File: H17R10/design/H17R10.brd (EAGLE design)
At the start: 60.6 x 60 mm, 94 parts, among them P1 HEXABIT__X3_NO_P1_P2_P3_P4_P5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, P4 PAD4, P5 PAD4, P6 PAD4, U1 STM32F091RBT6STMICROELECTRONI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, U3 TEXAS_INSTRUMENTS_ISO7741DBQR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, U4 TEXAS_INSTRUMENTS_ISO7742DBQR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, X1 XTALL_CSTCE8M00G52

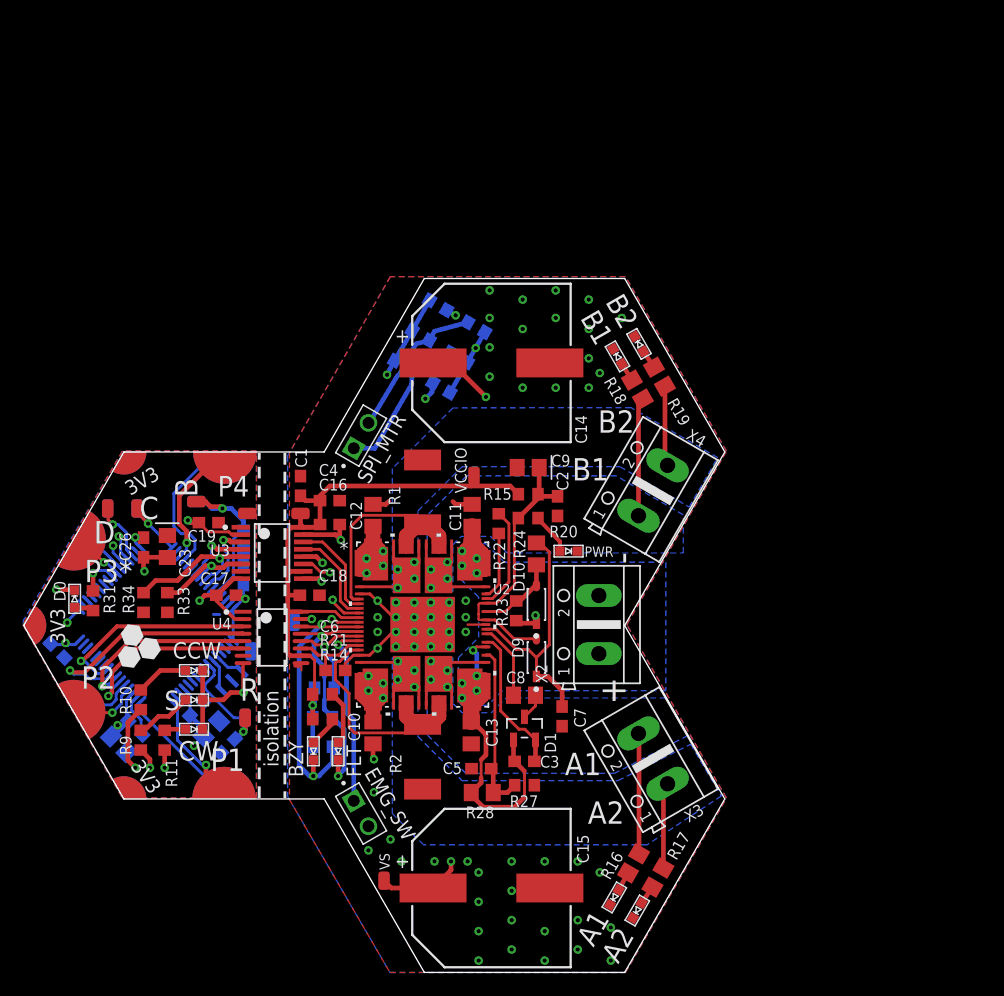
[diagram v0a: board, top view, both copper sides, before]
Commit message: -Changing the MCU to STM32G0B1CEU6N -Editing the electronic design -Editing the layout design to improve the performance
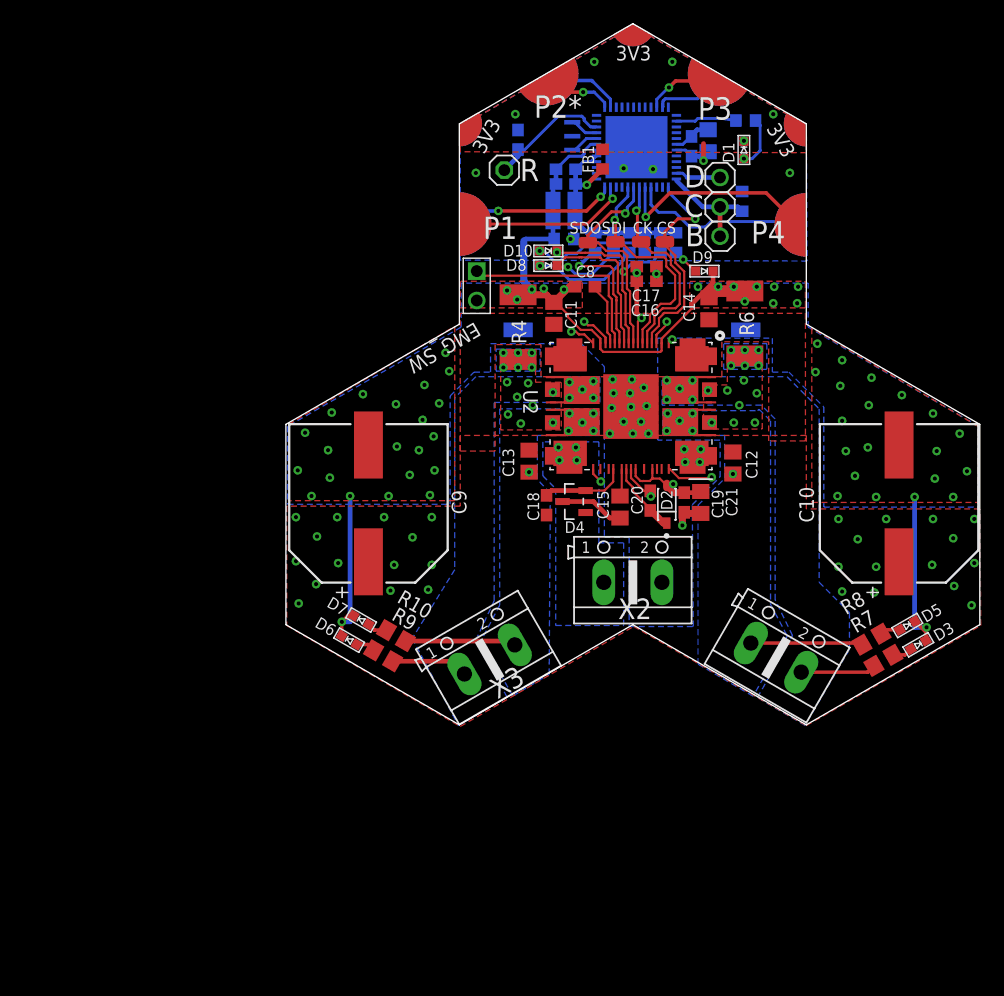
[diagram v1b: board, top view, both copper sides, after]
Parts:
- removed A1, A2, B1, B2, BZY: YELLOW, HEXABITZ_USER_INTERFACE_PARTS:VLMY1300-GS08
- removed B, C, D, R: PAD1, Hexabitz:PAD1
- removed C22: 1.00uF, Hexabitz:C-0805-POL
- removed C23, C24: 4.7uF, Hexabitz:C-0805-POL
- removed C25: 10nF, Hexabitz:C-0603
- removed C26, C27, C28, C29: 100nF, Hexabitz:C-0603
- removed CCW, CW, PWR: Green, HEXABITZ_USER_INTERFACE_PARTS:VLMTG1300-GS08
- removed D0, FLT, S: RED, HEXABITZ_USER_INTERFACE_PARTS:VLMS1300-GS08
- removed EMG_SW, SPI_MTR: 3-644456-2, HEXABITZ_USER_INTERFACE_PARTS:TE_3-644456-2
- removed P1: HEXABIT__X3_NO_P1_P2_P3_P4_P5_P6_P11_P12, hexabitz_connectors:HEXABIT_17.32_X3_NO_P1_P2_P3_P4_P5_P6_P11_P12
- removed P4, P5, P6, VCCIO, VCCIO1, VS: PAD4, HEXABITZ_CONNECTION_PARTS:PAD4
- removed R16, R17, R18, R19: 10k, HEXABITZ_RCLS:R-0805
- removed R20, R21: 330, HEXABITZ_RCLS:R-0603
- removed R22, R27, R33, R34: DNP, HEXABITZ_RCLS:R-0603
- removed R23: 0R, HEXABITZ_RCLS:R-0603
- removed R24, R28: DNP, HEXABITZ_RCLS:R-0805
- removed R25, R26: 39K, HEXABITZ_RCLS:R-0603
- removed R31: 270.0R, HEXABITZ_RCLS:R-0603
- removed R32: 10.0K, Hexabitz:R-0603
- removed U3: TEXAS_INSTRUMENTS_ISO7741DBQRTEXAS_INSTRUMENTS_ISO7741DBQR_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, HEXABITZ_ICs:TEXAS_INSTRUMENTS_ISO7741DBQR_0
- removed U4: TEXAS_INSTRUMENTS_ISO7742DBQRTEXAS_INSTRUMENTS_ISO7742DBQR_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, Texas Instruments - ISO7742DBQR:TEXAS_INSTRUMENTS_ISO7742DBQR_3
- added C20: 470nF, HEXABITZ_RCLS:C-0603
- added CK, CS, SDI, SDO: PAD4, HEXABITZ_CONNECTION_PARTS:PAD4
- added D2: STMICROELECTRONICS_BAT46ZFILMSTMICROELECTRONICS_BAT46ZFILM_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, HEXABITZ_RCLS:STMICROELECTRONICS_BAT46ZFILM_3
- added D3, D5, D6, D7: YELLOW, HEXABITZ_USER_INTERFACE_PARTS:VLMY1300-GS08
- added D4: STMICROELECTRONICS_BAR43SFILMSTMICROELECTRONICS_BAR43SFILM_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, HEXABITZ_RCLS:STMICROELECTRONICS_BAR43SFILM_0
- added D8: RED, HEXABITZ_USER_INTERFACE_PARTS:VLMS1300-GS08
- added FB1: (no value), HEXABITZ_RCLS:FB-TDK_MMZ1608Y300B
- added J1: 3-644456-2, HEXABITZ_USER_INTERFACE_PARTS:TE_3-644456-2
- added JP1: (no value), HEXABITZ_USER_INTERFACE_PARTS:1X01
- added JP2: (no value), pinhead:1X03
- added R12: 330, HEXABITZ_RCLS:R-0603
- added SJ1, SJ2: (no value), jumper:SJW
- added U$1: HEXABIT_17.32_X3_NO_P1_P2_P3_P4_P5_P6_P11_P12, hexabitz_connectors:HEXABIT_17.32_X3_NO_P1_P2_P3_P4_P5_P6_P11_P12
- C10: value 220nF -> 68uF; device HEXABITZ_RCLS:C-0805 -> HEXABITZ_RCLS:WCAP-ASLI_12.5X14(DXL)
- C14: value 68uF -> 220nF; device HEXABITZ_RCLS:WCAP-ASLI_12.5X14(DXL) -> HEXABITZ_RCLS:C-0805
- C15: value 68uF -> 47nF; device HEXABITZ_RCLS:WCAP-ASLI_12.5X14(DXL) -> HEXABITZ_RCLS:C-0805
- C18: value 100nF -> 470nF
- C19: value 100nF -> 220nF
- C2: value 220nF -> 100nF
- C21: value 100nF -> 22uF; device HEXABITZ_RCLS:C-0603 -> HEXABITZ_RCLS:C-0805-POL
- C3, C7: value 470nF -> 4.7uF; device HEXABITZ_RCLS:C-0603 -> HEXABITZ_RCLS:C-0805-POL
- C4: value 3.3nF -> 100nF
- C5: value DNP -> 1uF; device HEXABITZ_RCLS:C-0603 -> HEXABITZ_RCLS:C-0805-POL
- C8: value 47nF -> 100nF; device HEXABITZ_RCLS:C-0805 -> HEXABITZ_RCLS:C-0603
- C9: value 22uF -> 68uF; device HEXABITZ_RCLS:C-0805-POL -> HEXABITZ_RCLS:WCAP-ASLI_12.5X14(DXL)
- D1: value STMICROELECTRONICS_BAR43SFILMSTMICROELECTRONICS_BAR43SFILM_0_0 -> RED; device HEXABITZ_RCLS:STMICROELECTRONICS_BAR43SFILM_0 -> HEXABITZ_USER_INTERFACE_PARTS:VLMS1300-GS08
- D10: value STMICROELECTRONICS_BAT46ZFILMSTMICROELECTRONICS_BAT46ZFILM_0_3 -> YELLOW; device HEXABITZ_RCLS:STMICROELECTRONICS_BAT46ZFILM_3 -> HEXABITZ_USER_INTERFACE_PARTS:VLMY1300-GS08
- D9: value STMICROELECTRONICS_BAT46ZFILMSTMICROELECTRONICS_BAT46ZFILM_0_3 -> Green; device HEXABITZ_RCLS:STMICROELECTRONICS_BAT46ZFILM_3 -> HEXABITZ_USER_INTERFACE_PARTS:VLMTG1300-GS08
- R1: value 0R1 -> 0.0R; device HEXABITZ_RCLS:R2512 -> HEXABITZ_RCLS:R-0603
- R10, R9: value 270.0R -> 10k; device HEXABITZ_RCLS:R-0603 -> HEXABITZ_RCLS:R-0805
- R11: value 270.0R -> 330
- R14: value 330 -> 39K
- R15: value 0R -> 330
- R2: value 0R1 -> 270R; device HEXABITZ_RCLS:R2512 -> HEXABITZ_RCLS:R-0603
- R3: value 0R -> 10K
- R4, R6: value DNP -> 0R1; device HEXABITZ_RCLS:R-0603 -> HEXABITZ_RCLS:R2512
- R5: value DNP -> 39K
- R7: value DNP -> 10k; device HEXABITZ_RCLS:R-0603 -> HEXABITZ_RCLS:R-0805
- R8: value 0R -> 10k; device HEXABITZ_RCLS:R-0603 -> HEXABITZ_RCLS:R-0805
- U1: value STM32F091RBT6STMICROELECTRONICS_STM32F091RBT6_0_1 -> STM32G0B1CEU6NUFQFPN48_STM32_STM; device Hexabitz:STMICROELECTRONICS_STM32F091RBT6_1 -> HEXABITZ_ICs:UFQFPN48_STM32_STM
- U2: value (none) -> POWERSTEP01; device HEXABITZ_ICs:VFQFPN89_11X14X1_STM -> POWERSTEP01:IC_POWERSTEP01
- X1: value XTALL_CSTCE8M00G52 -> 8MHZ; device Hexabitz:XTALL_CSTCE8M00G52 -> HEXABITZ_OTHER_PARTS:XTALL_CSTCE8M00G52
- moved R2 61.7 mm to (9.76, 43.6), flipped to the bottom, turned to 0 degrees
- moved R11 58.9 mm to (-0.32, 33.0), flipped to the bottom, turned to 90 degrees
- moved U1 58.5 mm to (0.32, 41.3), turned to 180 degrees
- moved X1 55.5 mm to (-5.24, 42.2), turned to 180 degrees
- moved C6 54.8 mm to (5.08, 41.4), flipped to the bottom, turned to 270 degrees
- moved D1 53.5 mm to (9.60, 41.0), turned to 180 degrees
- moved C7 51.3 mm to (6.51, 41.8), flipped to the bottom, turned to 90 degrees
- moved R14 50.5 mm to (2.38, 33.0), flipped to the bottom, turned to 90 degrees
- moved C10 49.6 mm to (23.0, 10.5)
- moved C3 48.6 mm to (-5.95, 36.7), flipped to the bottom, turned to 0 degrees
- moved R13 48.1 mm to (-1.67, 33.0), turned to 90 degrees
- moved C5 47.9 mm to (-5.95, 34.9), flipped to the bottom, turned to 0 degrees
- moved C17 46.1 mm to (1.19, 31.0)
- moved C21 46.0 mm to (5.87, 10.6), flipped to the top, turned to 270 degrees
- moved R7 45.1 mm to (21.7, -3.10), flipped to the top
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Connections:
- removed net ADC_IN: C5.1, R27.2, R28.1, U2.54
- removed net B1: B.P$1, B.P$2, R32.2, U1.60
- removed net CK: U2.11, U3.13
- removed net CP: C8.1, U2.57
- removed net FORWARD: R10.2, U1.33
- removed net GND1: A1.C, A2.C, B1.C, B2.C, C1.2, C10.2, C11.2, C12.2, C13.2, C14.2, C15.2, C16.2, C18.2, C2.2, C4.2, C5.2, C6.2, C7.2, C9.2, EMG_SW.2, P6.P$1, PWR.C, R1.1, R2.1, R27.1, U2.21, U2.59, U2.8, U2.EPAD9, U3.15, U3.9, U4.15, U4.9, X2.2
- removed net MC_BUSY/SYNC: U1.25, U4.3
- removed net MC_CK: U1.55, U3.4
- removed net MC_CS: U1.58, U3.3
- removed net MC_FLAG: U1.24, U4.4
- removed net MC_MISO: R33.1, U1.56, U3.6
- removed net MC_MOSI: R34.1, U1.57, U3.5
- removed net MC_STBY/RESET: U1.22, U4.6
- removed net MS_STCK: U1.23, U4.5
- removed net N$11: R9.1, S.A
- removed net N$18: R3.1, U3.12
- removed net N$20: R4.1, R6.1, SPI_MTR.2
- removed net N$21: R5.1, R7.1, SPI_MTR.1
- removed net N$22: R22.2, U2.64
- removed net N$23: R22.1, U2.63
- removed net N$24: CCW.A, R10.1
- removed net N$25: CW.A, R11.1
- removed net N$3: R31.2, U1.41
- removed net N$7: D.P$1, D.P$2, U1.46
- removed net N$8: C7.1, D9.1, R24.1, U2.58
- removed net N$9: C.P$1, C.P$2, U1.49
- removed net R1: C21.1, R.P$1, R.P$2, U1.7
- removed net REVERSED: R11.2, U1.45
- removed net SENSE_A: R2.2, U2.20, U2.34, U2.35, U2.36, U2.39, U2.40, U2.41, U2.EPAD10, U2.EPAD11
- removed net SENSE_B: R1.2, U2.77, U2.78, U2.79, U2.82, U2.83, U2.84, U2.9, U2.EPAD12, U2.EPAD13
- removed net STBY/RESET: C6.1, U2.19, U4.11
- removed net STOPPED: R9.2, U1.44
- removed net UART1_RX*: P1.PAD_PD2, U1.43
- removed net UART1_TX*: P1.PAD_PU2, U1.42
- removed net UART2_RX*: P1.PAD_PD3, U1.17
- removed net UART2_TX*: P1.PAD_PU3, U1.16
- removed net UART3_RX: U1.30
- removed net UART3_TX: U1.29
- removed net UART4_RX: P1.PAD_PD8, U1.52
- removed net UART4_TX: P1.PAD_PU8, U1.51
- removed net UART6_RX: P1.PAD_PD1, U1.21
- removed net UART6_TX: P1.PAD_PU1, U1.20
- removed net UART7_RX: U1.9
- removed net UART7_TX: U1.8
- removed net UART8_RX: U1.11
- removed net UART8_TX: U1.10
- removed net VCCIO: C1.1, C16.1, C18.1, C4.1, R13.2, R14.2, R15.1, R21.2, R25.2, R26.2, U2.13, U3.10, U3.16, U4.10, U4.16, VCCIO.P$1, VCCIO1.P$1
- removed net VSREG: D10.2, R23.2, R24.2, U2.61
- removed net VSS: C10.1, C11.1, C12.1, C13.1, C14.1, C15.1, C3.2, D1.1, D10.1, R23.1, R28.2, U2.1, U2.2, U2.23, U2.24, U2.25, U2.26, U2.27, U2.28, U2.29, U2.3, U2.30, U2.31, U2.32, U2.4, U2.43, U2.44, U2.45, U2.46, U2.47, U2.48, U2.49, U2.5, U2.50, U2.51, U2.52, U2.55, U2.6, U2.66, U2.67, U2.68, U2.69, U2.70, U2.71, U2.72, U2.73, U2.74, U2.75, U2.86, U2.87, U2.88, U2.89, U2.EPAD1, U2.EPAD2, U2.EPAD5, U2.EPAD6, VS.P$1, X2.1
- removed net V_BOOT: C3.1, D1.2, U2.56
- new net C: JP2.1, JP2.2, R3.2, U1.36
- new net D: JP2.3, U1.35
- new net N$26: C18.2, D4.2, U2.56
- new net N$27: C20.1, D2.1, U2.58
- new net N$32: C15.2, D4.3
- new net RESET: C8.1, U2.19
- new net SCK: CK.P$1, U1.42, U2.11
- new net SENSEA: R4.2, SJ1.2, U2.20, U2.34, U2.39
- new net SENSEB: R6.2, SJ2.2, U2.77, U2.82, U2.9
- new net USART2_RX: U$1.PAD_PD1, U1.14
- new net USART2_TX: U$1.PAD_PU1, U1.13
- new net USART3_RX: U$1.PAD_PD2, U1.23
- new net USART3_TX: U$1.PAD_PU2, U1.22
- new net USART5_RX: U$1.PAD_PD8, U1.40
- new net USART5_TX: U$1.PAD_PU8, U1.41
- new net USART6_RX: U$1.PAD_PD3, U1.48
- new net USART6_TX: U$1.PAD_PU3, U1.47
- new net VDDA: C16.2, C17.2, C19.1, C2.2, C21.1, C3.1, C4.2, C5.1, D2.2, FB1.2, R11.2, R12.2, R13.2, R14.2, R15.2, R5.2, U1.4, U1.5, U1.6, U2.13, U2.60, U2.62
- new net VS: C10.1, C11.1, C12.1, C13.1, C14.1, C18.1, C9.1, D4.1, U2.1, U2.23, U2.43, U2.55, U2.61, U2.66, X2.1
- new net VSSA: C10.2, C11.2, C12.2, C13.2, C14.2, C16.1, C17.1, C19.2, C2.1, C20.2, C21.2, C3.2, C4.1, C5.2, C8.2, C9.2, D3.C, D5.C, D6.C, D7.C, D9.C, J1.2, R1.2, R4.1, R6.1, SJ1.1, SJ2.1, U1.7, U2.21, U2.59, U2.8, U2.EPAD9, X2.2
- net BUSY/SYNC: now also D10.C, R14.1; no longer BZY.C, R26.1, U4.14
- net CS: now also CS.P$1, U1.37; no longer U3.14
- net FLAG: now also D8.C; no longer FLT.C, U4.13
- net GND: now also C1.1, C6.1, C7.2, D1.C, R1.1, R3.1, U$1.PAD_PD12, U$1.PAD_PD17, U$1.PAD_PD19, U1.30, U1.49; no longer C17.2, C19.2, C21.2, C22.2, C23.2, C24.2, C25.2, C26.2, C27.2, C28.2, C29.2, CCW.C, CW.C, D0.C, P1.PAD_PD12, P1.PAD_PD17, P1.PAD_PD19, P5.P$1, R32.1, S.C, U1.12, U1.18, U1.31, U1.47, U1.53, U1.54, U1.63, U3.2, U3.8, U4.2, U4.8
- net N$1: now also U1.8, X1.P$1; no longer C2.1, C9.1, D9.2, R15.2, R20.2, U2.60, U2.62
- net N$10: now also D3.A, R7.1; no longer A1.A, R16.1
- net N$12: now also C1.2, JP1.1, U1.10; no longer BZY.A, R14.1
- net N$13: now also D8.A, R11.1; no longer FLT.A, R21.1
- net N$14: now also D9.A, R12.1; no longer PWR.A, R20.1
- net N$15: now also D5.A, R8.1; no longer A2.A, R17.1
- net N$16: now also D6.A, R9.1; no longer B1.A, R18.1
- net N$17: now also R2.2, U1.26; no longer B2.A, R19.1
- net N$19: now also D1.A, R2.1; no longer R8.1, U3.11
- net N$2: now also U1.9, X1.P$3; no longer C8.2, D1.3
- net N$4: now also C15.1, U2.57; no longer D0.A, R31.1
- net N$5: now also D10.A, R15.1; no longer U1.5, X1.P$1
- net N$6: now also D7.A, R10.1; no longer U1.6, X1.P$3
- net OUTA1: now also R10.2; no longer R16.2
- net OUTA2: now also R9.2; no longer R17.2
- net OUTB1: now also R8.2; no longer R18.2
- net OUTB2: now also R7.2; no longer R19.2
- net SDI: now also SDI.P$1, U1.44; no longer R3.2, R4.2, R5.2
- net SDO: now also SDO.P$1, U1.43; no longer R6.2, R7.2, R8.2
- net STCK: now also R5.1; no longer R25.1, U4.12
- net SW: now also J1.1; no longer EMG_SW.1
- net VDD: now also C6.2, C7.1, FB1.1, U$1.PAD_PU12, U$1.PAD_PU17, U$1.PAD_PU19, U1.31; no longer C17.1, C19.1, C22.1, C23.1, C24.1, C25.1, C26.1, C27.1, C28.1, C29.1, P1.PAD_PU12, P1.PAD_PU17, P1.PAD_PU19, P4.P$1, R33.2, R34.2, U1.1, U1.13, U1.19, U1.32, U1.48, U1.64, U3.1, U3.7, U4.1, U4.7
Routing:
- net VSSA: track 0.00 -> 114.4 mm, vias 0 -> 75
- net VSS: track 99.6 -> 0.00 mm, vias 20 -> 0
- net VDDA: track 0.00 -> 63.5 mm, vias 0 -> 4
- net VCCIO: track 59.8 -> 0.00 mm, vias 1 -> 0
- net GND: track 33.7 -> 3.36 mm, vias 5 -> 10
- net GND1: track 30.2 -> 0.00 mm, vias 66 -> 0
- net N$18: track 29.6 -> 0.00 mm, vias 2 -> 0
- net REVERSED: track 25.9 -> 0.00 mm, vias 2 -> 0
- net STOPPED: track 24.4 -> 0.00 mm, vias 2 -> 0
- net SENSE_A: track 23.9 -> 0.00 mm
- net FORWARD: track 22.3 -> 0.00 mm, vias 2 -> 0
- net N$8: track 22.1 -> 0.00 mm
- net SENSE_B: track 22.0 -> 0.00 mm
- net N$1: track 23.6 -> 2.52 mm
- net MC_FLAG: track 20.6 -> 0.00 mm, vias 1 -> 0
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- added copper zone on layer 15, net GND
- added copper zone on layer 15, net OUTA1
- added copper zone on layer 15, net OUTA2
- added copper zone on layer 15, net OUTB1
- added copper zone on layer 15, net OUTB2
- added copper zone on layer 1, net SENSEA
- added copper zone on layer 16, net SENSEA
- added copper zone on layer 2, net SENSEA
- added copper zone on layer 1, net SENSEB
- added copper zone on layer 16, net SENSEB
- added copper zone on layer 2, net SENSEB
- added copper zone on layer 1, net VS
- added copper zone on layer 15, net VS
- added copper zone on layer 16, net VS
- added copper zone on layer 2, net VS
- added copper zone on layer 1, net VSSA
- added copper zone on layer 15, net VSSA
- added copper zone on layer 16, net VSSA
- added copper zone on layer 2, net VSSA
- removed copper zone on layer 1, net GND1
- removed copper zone on layer 16, net GND1
- removed copper zone on layer 2, net GND1
- removed copper zone on layer 15, net VSS
- removed copper zone on layer 16, net VSS
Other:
- board size 60.6 x 60 mm -> 60 x 60.6 mm
- board text added: "EMG_SW"
- board text added: "P2*"
- board text removed: "+"
- board text removed: "-"
- board text removed: "A1"
- board text removed: "A2"
- board text removed: "B1"
- board text removed: "B2"
- board text removed: "H17R10"
- board text removed: "Motors board Res 1 - 3+8 2 1 3+6 2(top) 4+8 3 1 3+4 2 4+7 3(top) 5+8"
- board text removed: "Multi-motor onfiguration"
- board text removed: "P2"
- board text removed: "P3*"
- board text removed: "SDI"
- board text removed: "SDO"
- board text removed: "Total Thickness 1.6 mm --------------------------------------------------------- copper_top_l1.gbr : Top Conductor - Copper: Thickness 0.035 mm Dielectric - FR-4: Thickness 0.175 mm copper_inner_l2.gbr : GND Plane - Copper: Thickness 0.035 mm Dielectric - FR-4: Thickness 1.11 mm copper_inner_l3.gbr : VDD Plane - Copper: Thickness 0.035 mm Dielectric - FR-4: Thickness 0.175 mm copper_bottom_l4.gbr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"
- board text removed: "isolation"

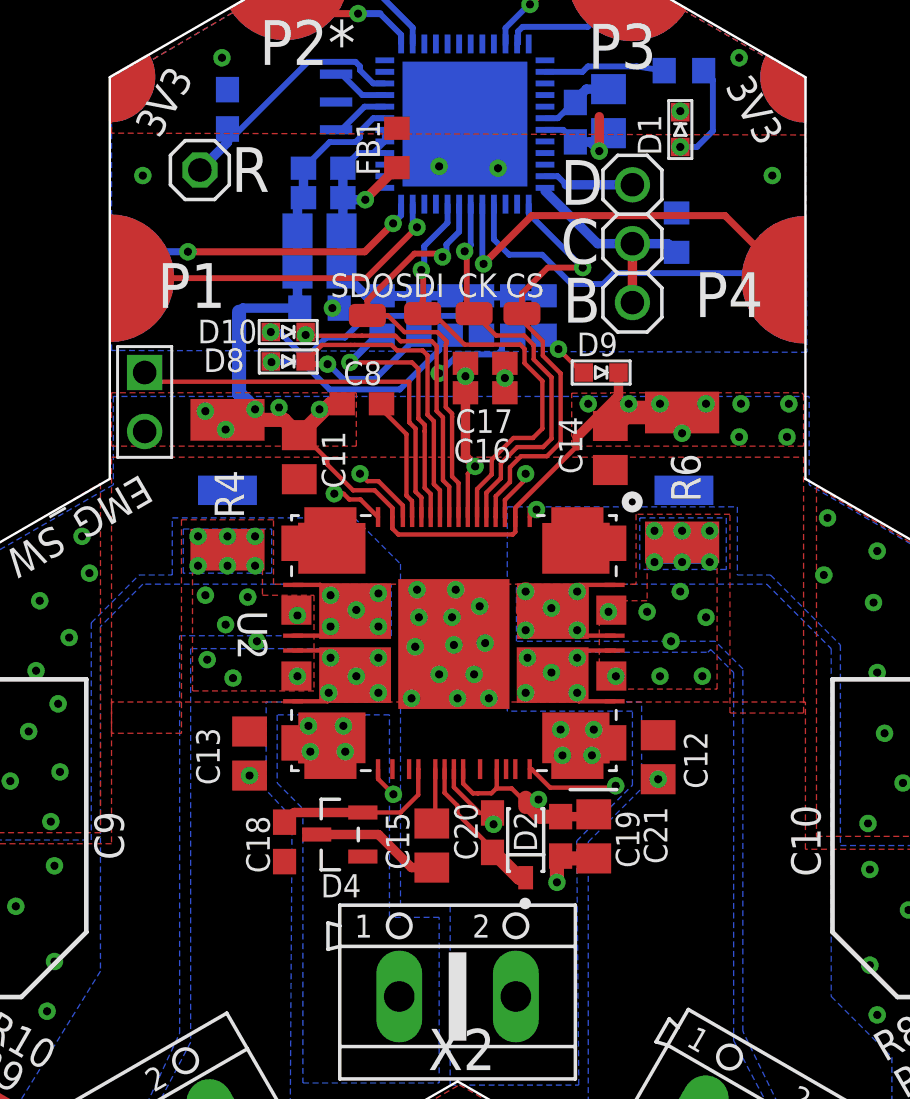
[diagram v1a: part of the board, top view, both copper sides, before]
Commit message: -Adding some components to the design to improve the performance
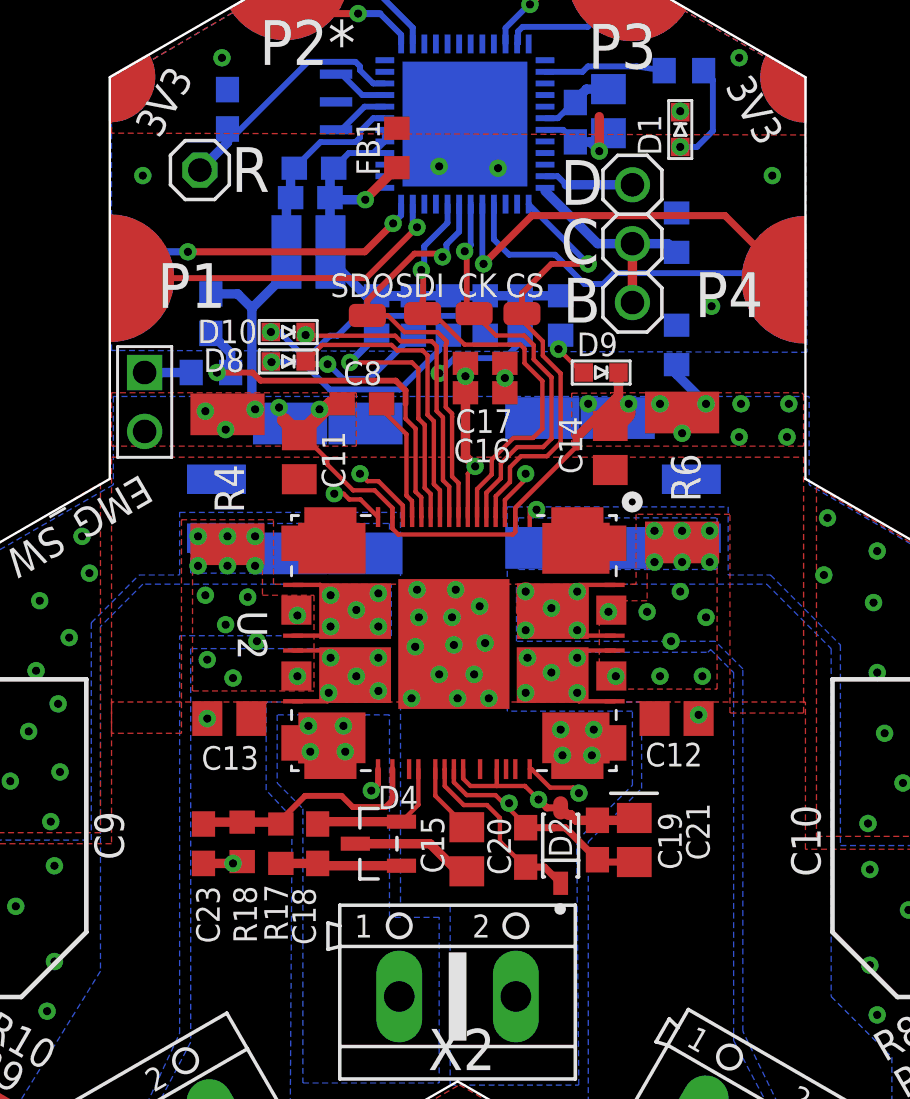
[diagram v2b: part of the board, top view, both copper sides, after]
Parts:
- added C22, C23: 100nF, HEXABITZ_RCLS:C-0603
- added R16: 1k, HEXABITZ_RCLS:R-0603
- added R17: 100k, HEXABITZ_RCLS:R-0603
- added R18: 2k, HEXABITZ_RCLS:R-0603
- added R19, R20, R21, R22: 0R1, HEXABITZ_RCLS:R2512
- moved R1 15.5 mm to (9.45, 31.8), turned to 270 degrees
- moved C12 1.85 mm to (9.45, 15.6), turned to 0 degrees
- moved C21 1.75 mm to (7.62, 10.4)
- moved C13 1.74 mm to (-9.84, 15.6), turned to 180 degrees
- moved D4 1.71 mm to (-3.41, 10.2)
- moved C19 1.60 mm to (6.03, 10.4)
- moved C20 1.56 mm to (2.94, 10.1)
- moved D2 1.53 mm to (4.45, 10.2)
- moved C15 1.52 mm to (0.40, 10.0)
- moved C18 1.43 mm to (-6.03, 10.2)
- moved R12 0.71 mm to (4.45, 33.0)
- moved SJ1 0.67 mm to (-10.4, 24.7)
- moved SJ2 0.57 mm to (10.1, 24.7)
- moved C4 0.56 mm to (-6.35, 38.1)
- moved C3 0.48 mm to (-6.43, 36.6)
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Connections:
- new net N$3: C22.1, R16.1, U2.18
- new net N$7: C23.1, R17.1, R18.2, U2.54
- net SENSEA: now also R19.2, R20.2
- net SENSEB: now also R21.2, R22.2
- net SW: now also R16.2; no longer U2.18
- net VS: now also R17.2
- net VSSA: now also C22.2, C23.2, R18.1, R19.1, R20.1, R21.1, R22.1
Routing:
- net N$3: track 0.00 -> 16.8 mm, vias 0 -> 1
- net SW: track 17.6 -> 2.01 mm
- net N$7: track 0.00 -> 10.5 mm
- net VS: track 0.58 -> 5.82 mm
- net VDDA: track 63.5 -> 66.4 mm
- net OUTB1: track 26.5 -> 24.7 mm
- net N$27: track 6.35 -> 8.06 mm
- net N$26: track 7.37 -> 6.22 mm
- net VSSA: track 114.4 -> 115.3 mm
- net N$4: track 2.41 -> 3.07 mm
- net OUTA1: track 23.6 -> 23.1 mm
